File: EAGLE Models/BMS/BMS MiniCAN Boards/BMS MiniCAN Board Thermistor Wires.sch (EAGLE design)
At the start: 46 parts, among them IC1 AT90CAN128, IC2 MCP2551SO8, IC3 NUP2105L, IC5 FT232RL, Q1 56P2859, X2 6_PIN_CONNMOLEX_HORI, X3 6_PIN_CONNMOLEX_HORI, X4 6_PIN_CONNMOLEX_HORI, X5 6_PIN_CONNMOLEX_HORI, X6 6_PIN_CONNMOLEX_HORI

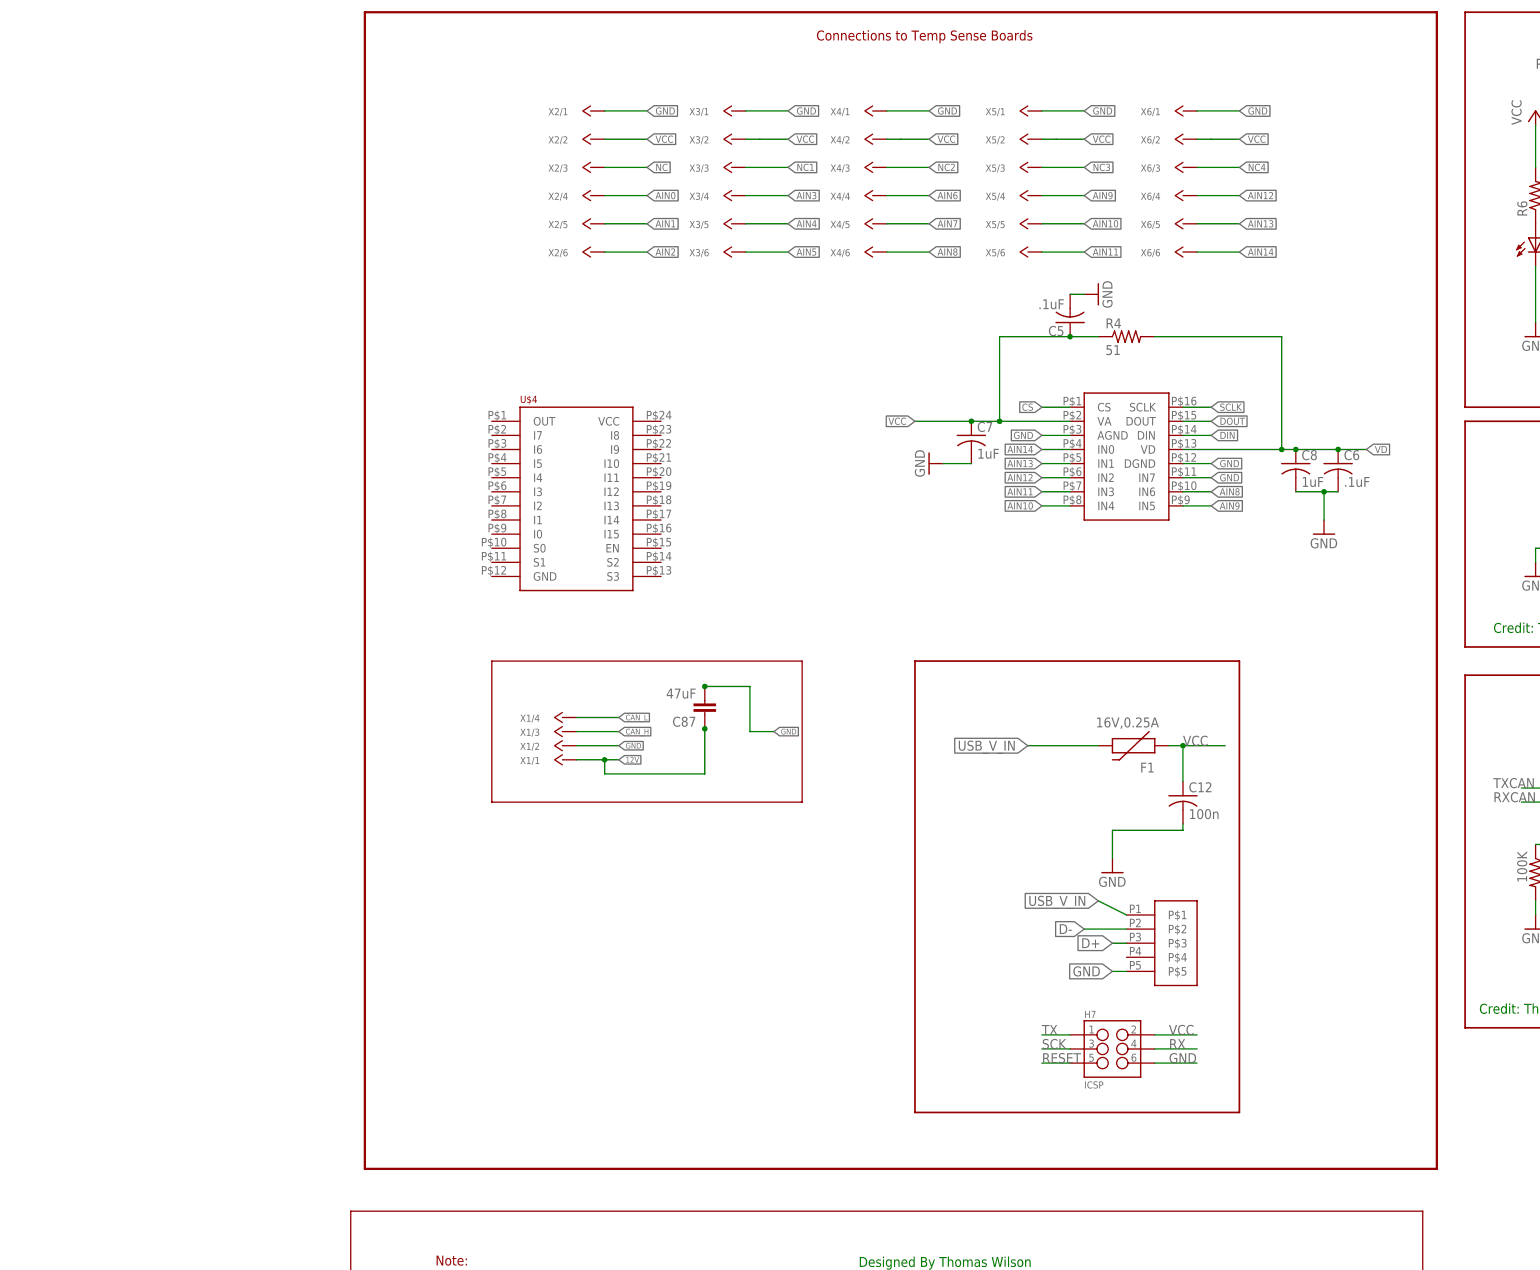
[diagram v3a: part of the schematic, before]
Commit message: Added All the Muxes
Added the muxes and their respective inputs/outputs.
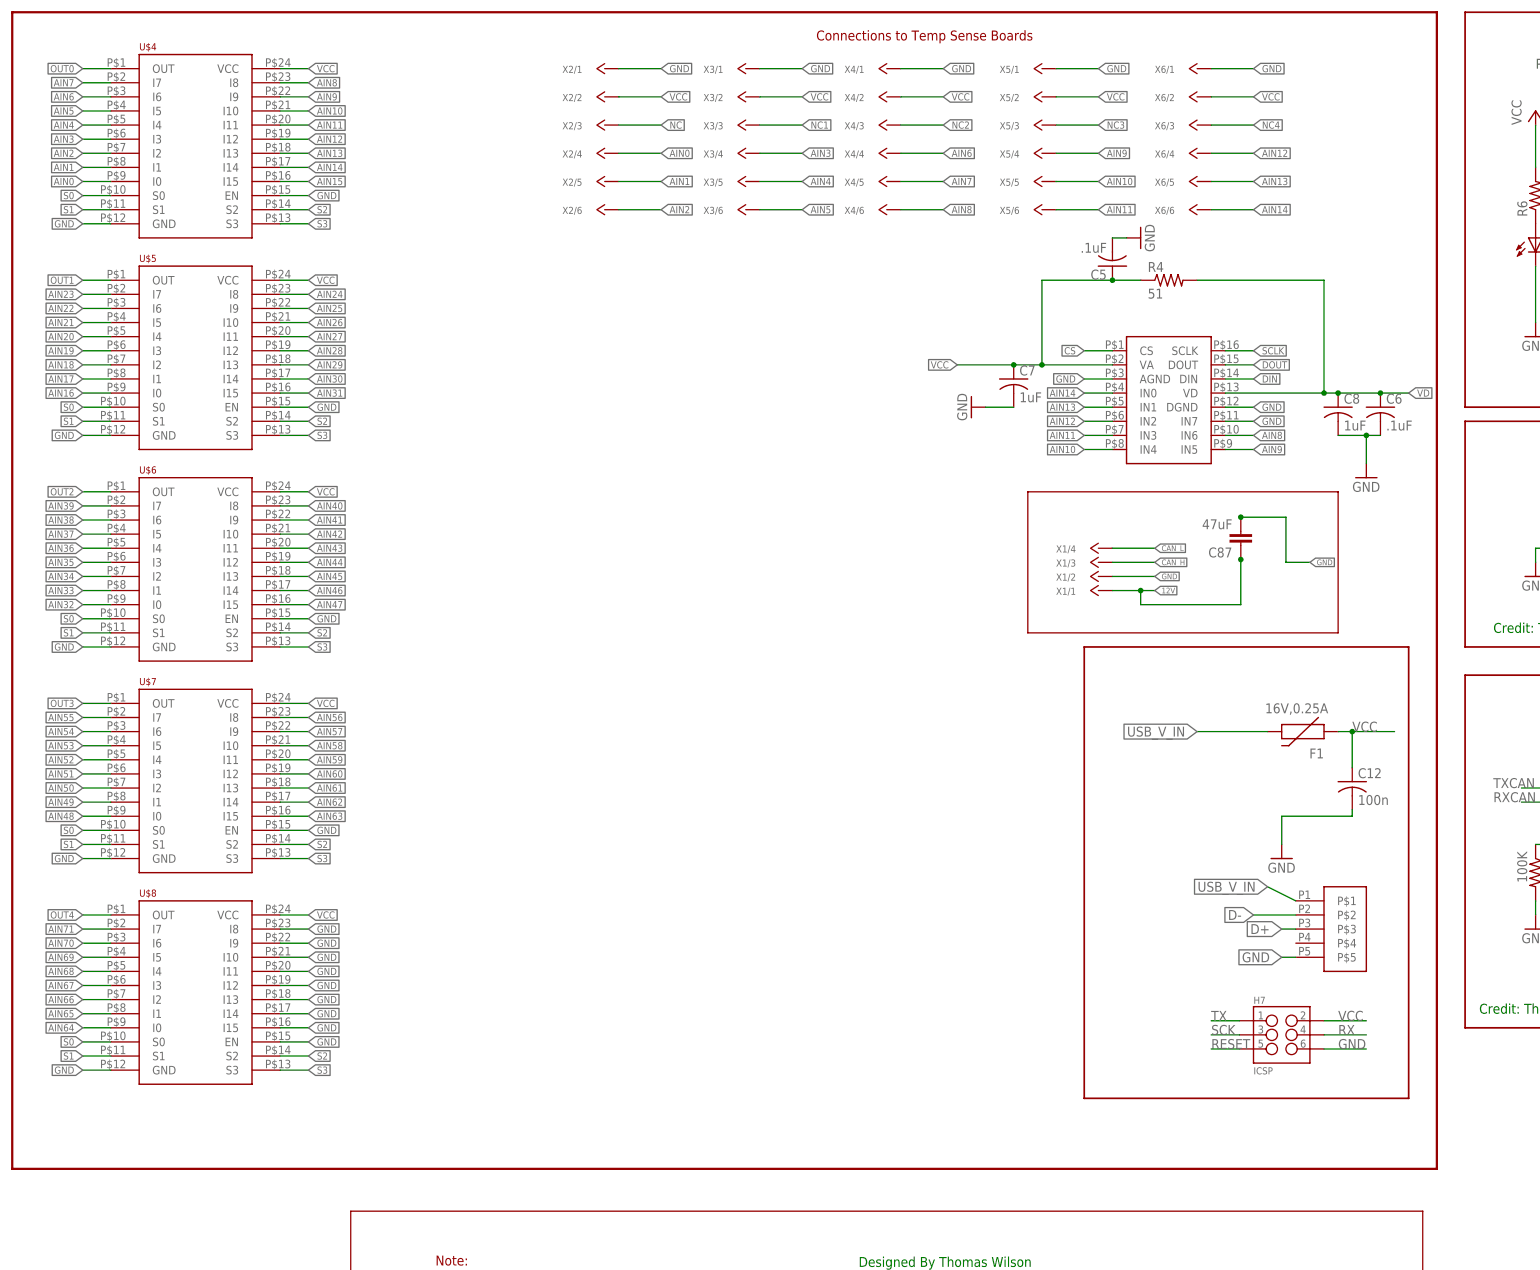
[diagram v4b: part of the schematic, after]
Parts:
- added U$5, U$6, U$7, U$8: CD74HC4067, BMS Lbr:CD74HC4067
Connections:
- new net AIN15: U$4.I15
- new net AIN16: U$5.I0
- new net AIN17: U$5.I1
- new net AIN18: U$5.I2
- new net AIN19: U$5.I3
- new net AIN20: U$5.I4
- new net AIN21: U$5.I5
- new net AIN22: U$5.I6
- new net AIN23: U$5.I7
- new net AIN24: U$5.I8
- new net AIN25: U$5.I9
- new net AIN26: U$5.I10
- new net AIN27: U$5.I11
- new net AIN28: U$5.I12
- new net AIN29: U$5.I13
- new net AIN30: U$5.I14
- new net AIN31: U$5.I15
- new net AIN32: U$6.I0
- new net AIN33: U$6.I1
- new net AIN34: U$6.I2
- new net AIN35: U$6.I3
- new net AIN36: U$6.I4
- new net AIN37: U$6.I5
- new net AIN38: U$6.I6
- new net AIN39: U$6.I7
- new net AIN40: U$6.I8
- new net AIN41: U$6.I9
- new net AIN42: U$6.I10
- new net AIN43: U$6.I11
- new net AIN44: U$6.I12
- new net AIN45: U$6.I13
- new net AIN46: U$6.I14
- new net AIN47: U$6.I15
- new net AIN48: U$7.I0
- new net AIN49: U$7.I1
- new net AIN50: U$7.I2
- new net AIN51: U$7.I3
- new net AIN52: U$7.I4
- new net AIN53: U$7.I5
- new net AIN54: U$7.I6
- new net AIN55: U$7.I7
- new net AIN56: U$7.I8
- new net AIN57: U$7.I9
- new net AIN58: U$7.I10
- new net AIN59: U$7.I11
- new net AIN60: U$7.I12
- new net AIN61: U$7.I13
- new net AIN62: U$7.I14
- new net AIN63: U$7.I15
- new net AIN64: U$8.I0
- new net AIN65: U$8.I1
- new net AIN66: U$8.I2
- new net AIN67: U$8.I3
- new net AIN68: U$8.I4
- new net AIN69: U$8.I5
- new net AIN70: U$8.I6
- new net AIN71: U$8.I7
- new net OUT0: U$4.OUT
- new net OUT1: U$5.OUT
- new net OUT2: U$6.OUT
- new net OUT3: U$7.OUT
- new net OUT4: U$8.OUT
- new net S0: U$4.S0, U$5.S0, U$6.S0, U$7.S0, U$8.S0
- new net S1: U$4.S1, U$5.S1, U$6.S1, U$7.S1, U$8.S1
- new net S2: U$4.S2, U$5.S2, U$6.S2, U$7.S2, U$8.S2
- new net S3: U$4.S3, U$5.S3, U$6.S3, U$7.S3, U$8.S3
- net AIN0: now also U$4.I0
- net AIN1: now also U$4.I1
- net AIN10: now also U$4.I10
- net AIN11: now also U$4.I11
- net AIN12: now also U$4.I12
- net AIN13: now also U$4.I13
- net AIN14: now also U$4.I14
- net AIN2: now also U$4.I2
- net AIN3: now also U$4.I3
- net AIN4: now also U$4.I4
- net AIN5: now also U$4.I5
- net AIN6: now also U$4.I6
- net AIN7: now also U$4.I7
- net AIN8: now also U$4.I8
- net AIN9: now also U$4.I9
- net GND: now also U$4.EN, U$4.GND, U$5.EN, U$5.GND, U$6.EN, U$6.GND, U$7.EN, U$7.GND, U$8.EN, U$8.GND, U$8.I10, U$8.I11, U$8.I12, U$8.I13, U$8.I14, U$8.I15, U$8.I8, U$8.I9
- net VCC: now also U$4.VCC, U$5.VCC, U$6.VCC, U$7.VCC, U$8.VCC
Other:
- moved on the sheet: C12, C5, C6, C7, C8, C87, F1, H7, R4, U$4, X1/1, X1/2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

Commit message: Added Resistors and Changed MCU I/O
Added 0603 package 10k resistors and connected muxes to the MCU
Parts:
- added R10, R11, R12, R13, R14, R15, R16, R17, R18, R19, R20, R21, R22, R23, R24, R25, R26, R27, R28, R29, R30, R31, R32, R5: 10K, adafruit:R-US_R0603
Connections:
- removed net CS0: IC1.(A8)PC0
- removed net CS1: IC1.(A9)PC1
- removed net CS2: IC1.(A10)PC2
- removed net CS3: IC1.(A11)PC3
- removed net SCK: H7.3
- net AIN0: no longer IC1.PF0(ADC0)
- net AIN1: no longer IC1.PF1(ADC1)
- net AIN2: no longer IC1.PF2(ADC2)
- net AIN3: no longer IC1.PF3(ADC3)
- net AIN4: no longer IC1.PF4(ADC4/TCK)
- net AIN5: no longer IC1.PF5(ADC5/TMS)
- net AIN6: no longer IC1.PF6(ADC6/TDO)
- net AIN7: no longer IC1.PF7(ADC7/TDI)
- net AVR_SCK: now also H7.3
- net GND: now also IC1.PF5(ADC5/TMS), IC1.PF6(ADC6/TDO), IC1.PF7(ADC7/TDI), R10.2, R11.2, R12.2, R13.2, R14.2, R15.2, R16.2, R17.2, R18.2, R19.2, R20.2, R21.2, R22.2, R23.2, R24.2, R25.2, R26.2, R27.2, R28.2, R29.2, R30.2, R31.2, R32.2, R5.2
- net OUT0: now also IC1.PF0(ADC0)
- net OUT1: now also IC1.PF1(ADC1)
- net OUT2: now also IC1.PF2(ADC2)
- net OUT3: now also IC1.PF3(ADC3)
- net OUT4: now also IC1.PF4(ADC4/TCK)
- net S0: now also IC1.(A8)PC0
- net S1: now also IC1.(A9)PC1
- net S2: now also IC1.(A10)PC2
- net S3: now also IC1.(A11)PC3
